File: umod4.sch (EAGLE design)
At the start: 101 parts, among them IC1 27C256-FEED-THRU, M1 Generic single-sided NEO-8, M2 RPi Pico W, Q1 DNP/SI2301CDS, Q2 SS8050, U1 RP2040, U2 W25Q128JVSIQ, U3 SY6280AAC, U4 74LVC2G04, U5 74LVC541, U6 74LVC541, U7 74LVC4245, U8 TLV75733P, Y1 12MHz

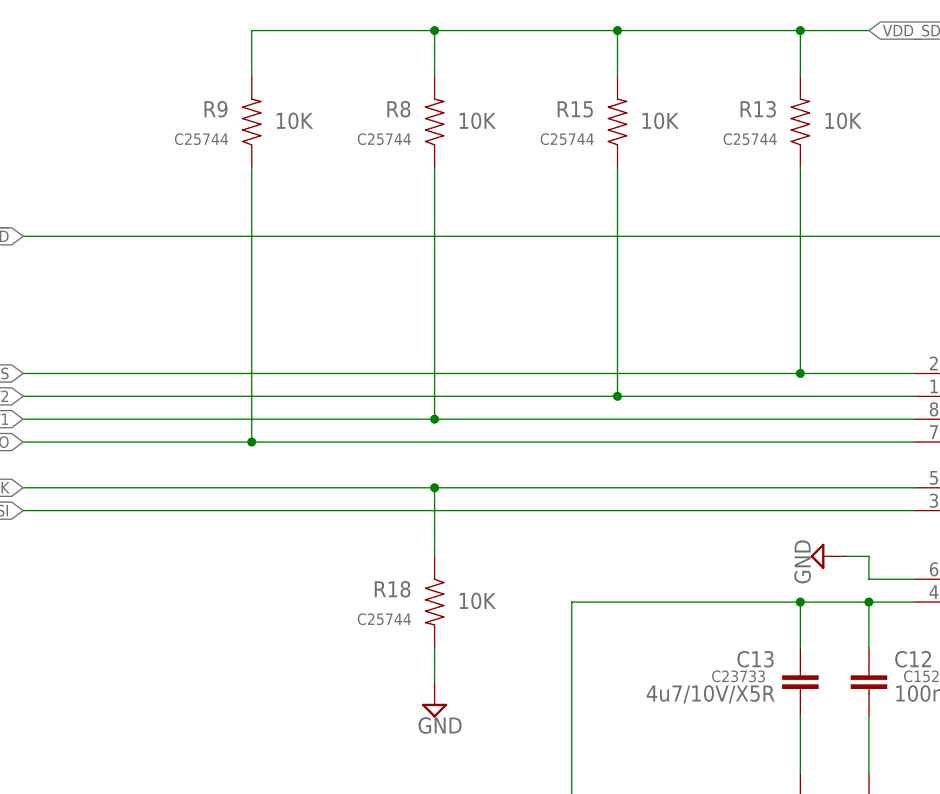
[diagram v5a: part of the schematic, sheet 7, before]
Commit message: Replace 10K 0402 packages with SMD-0603-NOM
- Affected parts: R3, R5, R7, R8. R9, R11, R12, R13, R15, R16, R17, R18, R19, R22, R25, R26
- LCSC_PART changed to C25804 (10K 0603 1% basic)
- Manually reworked wire angles on board to clear DRC failures from the new pad geometry
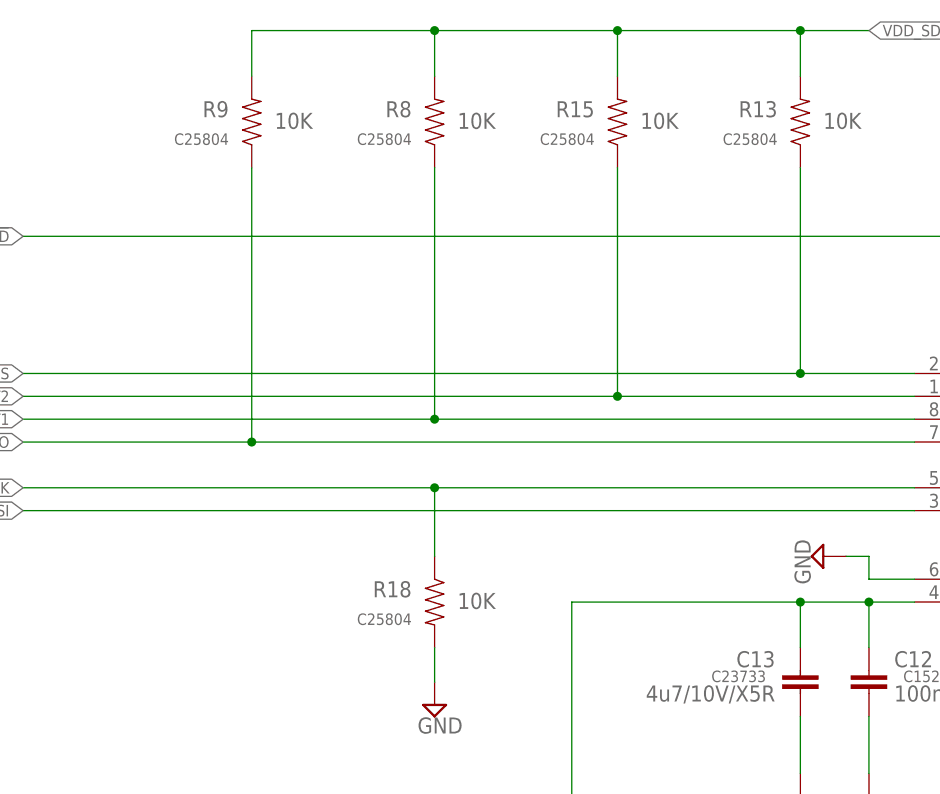
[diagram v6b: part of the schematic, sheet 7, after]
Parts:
- R11, R12, R13, R15, R16, R17, R18, R19, R22, R25, R26, R3, R5, R7, R8, R9: device SparkFun-03-01-2010:RESISTOR0402-RES -> robins-v7:RES-0603-NOM; LCSC_PART C25744 -> C25804

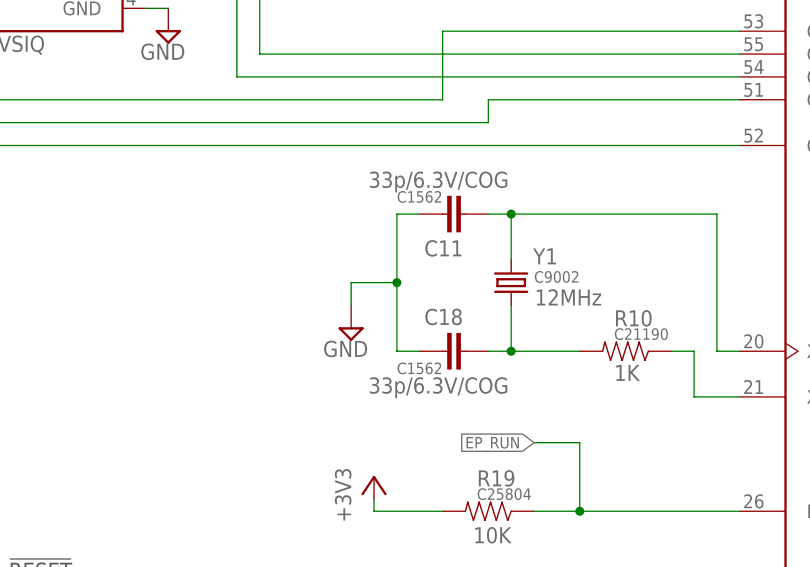
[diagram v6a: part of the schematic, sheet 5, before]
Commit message: Replace 33pF 0402 packages with SMD-0402-NOM
- Affected parts: C11, C18
- LCSC_PART unchanged
- Manually reworked wire angles on board to clear DRC failures from the new pad geometry
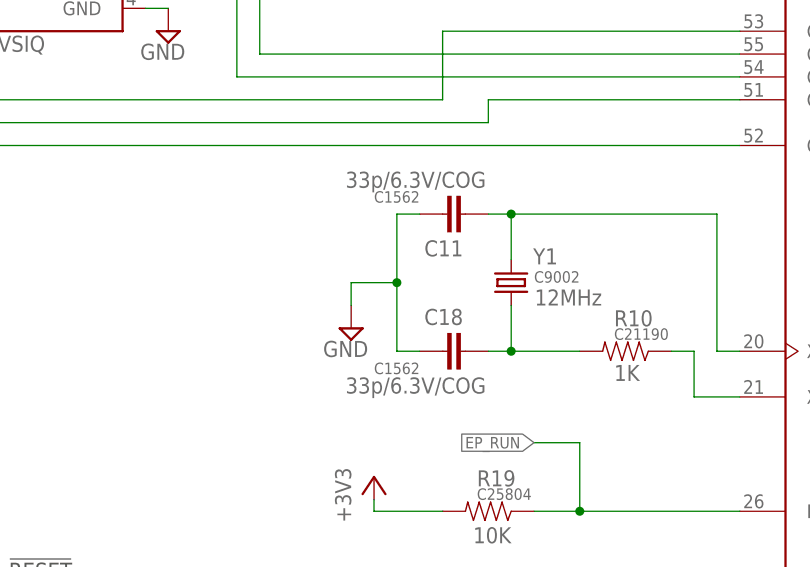
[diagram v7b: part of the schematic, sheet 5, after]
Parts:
- C11, C18: device SparkFun-03-01-2010:CAP0402-CAP -> robins-v7:CAP-0402-NOM
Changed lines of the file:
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@@
 <grid distance="0.1" unitdist="inch" unit="inch" style="lines" multiple="1" display="no" altdistance="0.01" altunitdist="inch" altunit="inch"/>
 <layers>
-<layer number="1" name="Top" color="4" fill="1" visible="yes" active="no"/>
-<layer number="2" name="Route2" color="1" fill="3" visible="yes" active="no"/>
-<layer number="3" name="Route3" color="4" fill="3" visible="yes" active="no"/>
-<layer number="14" name="Route14" color="1" fill="6" visible="yes" active="no"/>
-<layer number="15" name="Route15" color="4" fill="6" visible="yes" active="no"/>
-<layer number="16" name="Bottom" color="1" fill="1" visible="yes" active="no"/>
-<layer number="17" name="Pads" color="2" fill="1" visible="yes" active="no"/>
-<layer number="18" name="Vias" color="2" fill="1" visible="yes" active="no"/>
-<layer number="19" name="Unrouted" color="6" fill="1" visible="yes" active="no"/>
-<layer number="20" name="Dimension" color="15" fill="1" visible="yes" active="no"/>
-<layer number="21" name="tPlace" color="7" fill="1" visible="yes" active="no"/>
-<layer number="22" name="bPlace" color="7" fill="1" visible="yes" active="no"/>
-<layer number="23" name="tOrigins" color="15" fill="1" visible="yes" active="no"/>
-<layer number="24" name="bOrigins" color="15" fill="1" visible="yes" active="no"/>
-<layer number="25" name="tNames" color="7" fill="1" visible="yes" active="no"/>
-<layer number="26" name="bNames" color="7" fill="1" visible="yes" active="no"/>
-<layer number="27" name="tValues" color="7" fill="1" visible="yes" active="no"/>
-<layer number="28" name="bValues" color="7" fill="1" visible="yes" active="no"/>
+<layer number="1" name="Top" color="4" fill="1" visible="no" active="no"/>
+<layer number="2" name="Route2" color="1" fill="3" visible="no" active="no"/>
+<layer number="3" name="Route3" color="4" fill="3" visible="no" active="no"/>
+<layer number="14" name="Route14" color="1" fill="6" visible="no" active="no"/>
+<layer number="15" name="Route15" color="4" fill="6" visible="no" active="no"/>
+<layer number="16" name="Bottom" color="1" fill="1" visible="no" active="no"/>
+<layer number="17" name="Pads" color="2" fill="1" visible="no" active="no"/>
+<layer number="18" name="Vias" color="2" fill="1" visible="no" active="no"/>
+<layer number="19" name="Unrouted" color="6" fill="1" visible="no" active="no"/>
+<layer number="20" name="Dimension" color="15" fill="1" visible="no" active="no"/>
+<layer number="21" name="tPlace" color="7" fill="1" visible="no" active="no"/>
+<layer number="22" name="bPlace" color="7" fill="1" visible="no" active="no"/>
+<layer number="23" name="tOrigins" color="15" fill="1" visible="no" active="no"/>
+<layer number="24" name="bOrigins" color="15" fill="1" visible="no" active="no"/>
+<layer number="25" name="tNames" color="7" fill="1" visible="no" active="no"/>
+<layer number="26" name="bNames" color="7" fill="1" visible="no" active="no"/>
+<layer number="27" name="tValues" color="7" fill="1" visible="no" active="no"/>
+<layer number="28" name="bValues" color="7" fill="1" visible="no" active="no"/>
 <layer number="29" name="tStop" color="7" fill="3" visible="no" active="no"/>
 <layer number="30" name="bStop" color="7" fill="6" visible="no" active="no"/>
@@
 <layer number="35" name="tGlue" color="7" fill="4" visible="no" active="no"/>
 <layer number="36" name="bGlue" color="7" fill="5" visible="no" active="no"/>
-<layer number="37" name="tTest" color="7" fill="1" visible="yes" active="no"/>
-<layer number="38" name="bTest" color="7" fill="1" visible="yes" active="no"/>
+<layer number="37" name="tTest" color="7" fill="1" visible="no" active="no"/>
+<layer number="38" name="bTest" color="7" fill="1" visible="no" active="no"/>
 <layer number="39" name="tKeepout" color="4" fill="11" visible="no" active="no"/>
 <layer number="40" name="bKeepout" color="1" fill="11" visible="no" active="no"/>
@@
 <layer number="44" name="Drills" color="7" fill="1" visible="no" active="no"/>
 <layer number="45" name="Holes" color="7" fill="1" visible="no" active="no"/>
-<layer number="46" name="Milling" color="3" fill="1" visible="yes" active="no"/>
-<layer number="47" name="Measures" color="7" fill="1" visible="yes" active="no"/>
-<layer number="48" name="Document" color="7" fill="1" visible="yes" active="no"/>
-<layer number="49" name="Reference" color="7" fill="1" visible="yes" active="no"/>
-<layer number="50" name="dxf" color="7" fill="1" visible="yes" active="no"/>
-<layer number="51" name="tDocu" color="7" fill="1" visible="yes" active="no"/>
-<layer number="52" name="bDocu" color="7" fill="1" visible="yes" active="no"/>
-<layer number="53" name="tGND_GNDA" color="7" fill="9" visible="yes" active="no"/>
-<layer number="54" name="bGND_GNDA" color="1" fill="9" visible="yes" active="no"/>
-<layer number="56" name="wert" color="7" fill="1" visible="yes" active="no"/>
-<layer number="57" name="tCAD" color="7" fill="1" visible="yes" active="no"/>
-<layer number="59" name="tCarbon" color="7" fill="1" visible="yes" active="no"/>
-<layer number="60" name="bCarbon" color="7" fill="1" visible="yes" active="no"/>
+<layer number="46" name="Milling" color="3" fill="1" visible="no" active="no"/>
+<layer number="47" name="Measures" color="7" fill="1" visible="no" active="no"/>
+<layer number="48" name="Document" color="7" fill="1" visible="no" active="no"/>
+<layer number="49" name="Reference" color="7" fill="1" visible="no" active="no"/>
+<layer number="50" name="dxf" color="7" fill="1" visible="no" active="no"/>
+<layer number="51" name="tDocu" color="7" fill="1" visible="no" active="no"/>
+<layer number="52" name="bDocu" color="7" fill="1" visible="no" active="no"/>
+<layer number="53" name="tGND_GNDA" color="7" fill="9" visible="no" active="no"/>
+<layer number="54" name="bGND_GNDA" color="1" fill="9" visible="no" active="no"/>
+<layer number="56" name="wert" color="7" fill="1" visible="no" active="no"/>
+<layer number="57" name="tCAD" color="7" fill="1" visible="no" active="no"/>
+<layer number="59" name="tCarbon" color="7" fill="1" visible="no" active="no"/>
+<layer number="60" name="bCarbon" color="7" fill="1" visible="no" active="no"/>
 <layer number="88" name="SimResults" color="9" fill="1" visible="yes" active="yes"/>
 <layer number="89" name="SimProbes" color="9" fill="1" visible="yes" active="yes"/>
@@
 <attribute name="LCSC_PART" value="C21190"/>
 </part>
-<part name="C11" library="SparkFun-03-01-2010" deviceset="CAP" device="0402-CAP" value="33p/6.3V/COG">
+<part name="C11" library="robins-v7" deviceset="CAP" device="-0402-NOM" value="33p/6.3V/COG">
 <attribute name="LCSC_PART" value="C1562"/>
 </part>
-<part name="C18" library="SparkFun-03-01-2010" deviceset="CAP" device="0402-CAP" value="33p/6.3V/COG">
+<part name="C18" library="robins-v7" deviceset="CAP" device="-0402-NOM" value="33p/6.3V/COG">
 <attribute name="LCSC_PART" value="C1562"/>
 </part>
@@
 <attribute name="LCSC_PART" x="130.81" y="95.25" size="1.27" layer="96"/>
 </instance>
-<instance part="C11" gate="G$1" x="114.3" y="109.22" smashed="yes" rot="R90">
+<instance part="C11" gate="G$1" x="111.76" y="109.22" smashed="yes" rot="R90">
 <attribute name="NAME" x="114.046" y="106.299" size="1.778" layer="95" rot="R180"/>
-<attribute name="VALUE" x="119.126" y="113.919" size="1.778" layer="96" rot="R180"/>
-<attribute name="LCSC_PART" x="111.76" y="111.76" size="1.27" layer="96" rot="R180"/>
-</instance>
-<instance part="C18" gate="G$1" x="114.3" y="93.98" smashed="yes" rot="R90">
+<attribute name="VALUE" x="116.586" y="113.919" size="1.778" layer="96" rot="R180"/>
+<attribute name="LCSC_PART" x="109.22" y="111.76" size="1.27" layer="96" rot="R180"/>
+</instance>
+<instance part="C18" gate="G$1" x="111.76" y="93.98" smashed="yes" rot="R90">
 <attribute name="NAME" x="114.046" y="98.679" size="1.778" layer="95" rot="R180"/>
-<attribute name="VALUE" x="119.126" y="91.059" size="1.778" layer="96" rot="R180"/>
-<attribute name="LCSC_PART" x="111.76" y="92.71" size="1.27" layer="96" rot="R180"/>
+<attribute name="VALUE" x="116.586" y="91.059" size="1.778" layer="96" rot="R180"/>
+<attribute name="LCSC_PART" x="109.22" y="92.71" size="1.27" layer="96" rot="R180"/>
 </instance>
 <instance part="V6" gate="GND" x="101.6" y="96.52" rot="MR0"/>
@@
 <segment>
 <pinref part="Y1" gate="G$1" pin="1"/>
-<wire x1="119.38" y1="93.98" x2="119.38" y2="99.06" width="0.1524" layer="91"/>
 <pinref part="R10" gate="G$1" pin="2"/>
 <wire x1="127" y1="93.98" x2="119.38" y2="93.98" width="0.1524" layer="91"/>
 <pinref part="C18" gate="G$1" pin="2"/>
 <wire x1="119.38" y1="93.98" x2="116.84" y2="93.98" width="0.1524" layer="91"/>
+<wire x1="119.38" y1="99.06" x2="119.38" y2="93.98" width="0.1524" layer="91"/>
 <junction x="119.38" y="93.98"/>
 </segment>
@@
 <wire x1="142.24" y1="93.98" x2="144.78" y2="93.98" width="0.1524" layer="91"/>
 <pinref part="Y1" gate="G$1" pin="2"/>
-<wire x1="119.38" y1="104.14" x2="119.38" y2="109.22" width="0.1524" layer="91"/>
 <wire x1="142.24" y1="109.22" x2="119.38" y2="109.22" width="0.1524" layer="91"/>
 <pinref part="C11" gate="G$1" pin="2"/>
 <wire x1="119.38" y1="109.22" x2="116.84" y2="109.22" width="0.1524" layer="91"/>
+<wire x1="119.38" y1="104.14" x2="119.38" y2="109.22" width="0.1524" layer="91"/>
 <junction x="119.38" y="109.22"/>
 </segment>
